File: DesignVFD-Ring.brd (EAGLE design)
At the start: 160 x 100 mm, 33 parts, among them IC1 LMR64010XMF/NOPB, IC2 LM340S-05, J1 NPPN081BFLD-RC, J2 NPPN081BFLD-RC, J3 NPPN081BFLD-RC, J4 NPPN081BFLD-RC, U1 MAX6920AWP+, U2 LM1084IS-5.0, U3 TPS76325DBVT

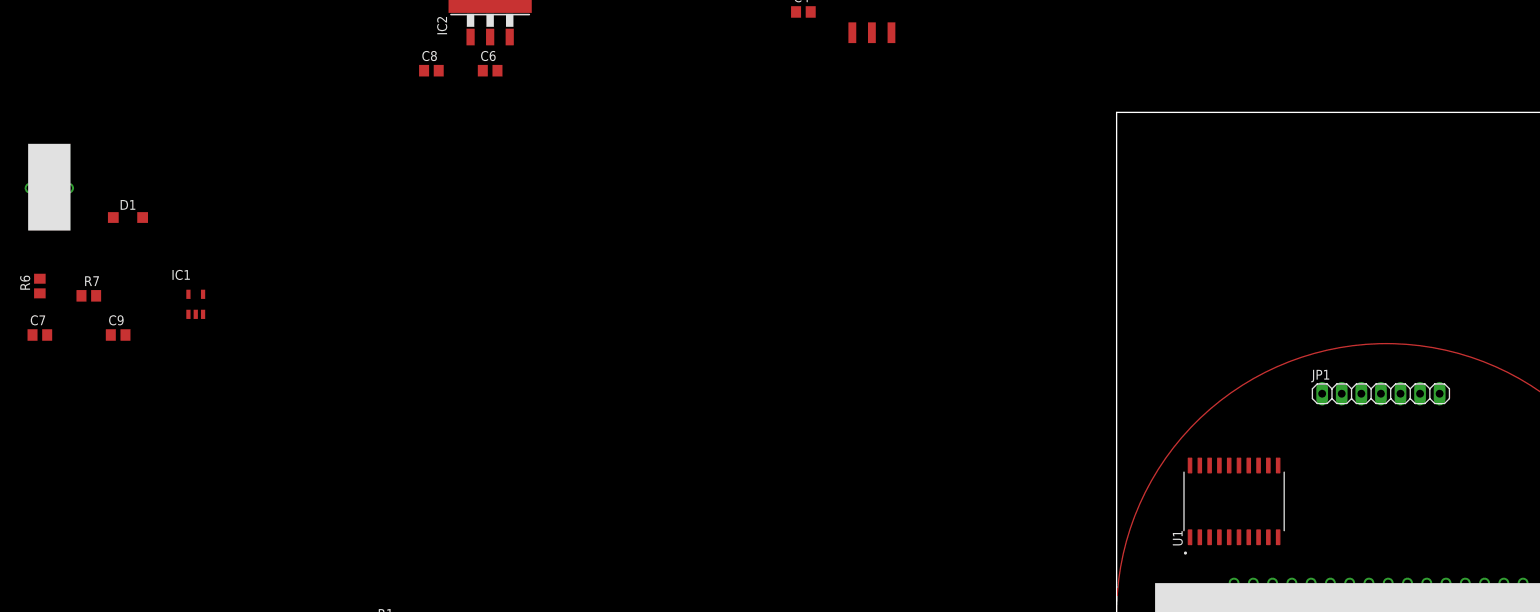
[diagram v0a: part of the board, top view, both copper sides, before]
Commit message: 24V reg layout
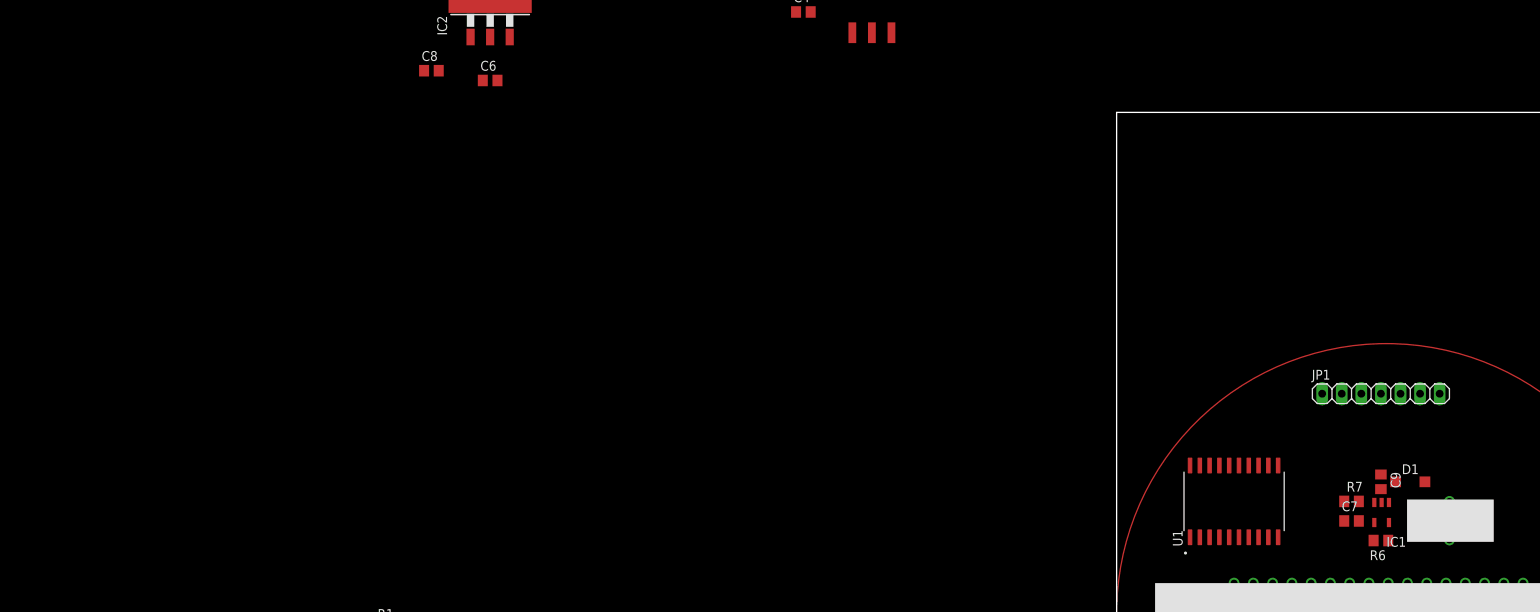
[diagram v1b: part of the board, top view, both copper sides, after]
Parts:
- moved U$1 188.6 mm to (43.2, 49.5), turned to 270 degrees
- moved R6 177.1 mm to (34.3, 44.5), turned to 180 degrees
- moved C7 171.9 mm to (30.5, 47.0)
- moved D1 169.9 mm to (38.1, 52.1)
- moved R7 166.0 mm to (30.5, 49.5)
- moved C9 164.9 mm to (34.3, 52.1), turned to 270 degrees
- moved IC1 156.0 mm to (34.3, 48.3), turned to 180 degrees
- moved C6 1.27 mm to (-81.3, 104.1)

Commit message: Replaced headers with Teensy device
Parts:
- removed J1, J2, J3, J4: NPPN081BFLD-RC, NPPN081BFLD-RC:SULLINS_NPPN081BFLD-RC
- added U$3: TEENSY-3.2, FormE:TEENSY3.2
- moved R2 35.1 mm to (57.1, 47.0)
- moved R3 31.7 mm to (61.0, 45.7), flipped to the bottom, turned to 270 degrees
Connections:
- net +3V3: now also U$3.3V3+; no longer J3.3
- net +5V: now also U$3.VIN; no longer J3.1
- net GND: now also U$3.AGND, U$3.GND; no longer J1.1, J3.2
- net T_BLANK: now also U$3.9; no longer J3.4
- net T_CS2: now also U$3.5; no longer J1.5
- net T_HEATER_CTL: now also U$3.21; no longer J3.6
- net T_IGN_INPUT: now also U$3.7; no longer J1.8
- net T_LIGHT_INPUT: now also U$3.15; no longer J4.4
- net T_MOSI: now also U$3.11; no longer J2.5
- net T_MOSI2: now also U$3.3; no longer J1.4
- net T_SCK: now also U$3.13; no longer J4.6
- net T_SCK2: now also U$3.1; no longer J1.3

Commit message: Initial layout complete
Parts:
- moved C2 177.0 mm to (49.5, 63.8), flipped to the bottom
- moved D3 166.8 mm to (50.8, 59.2)
- moved D2 165.7 mm to (50.8, 55.1)
- moved OK1 164.8 mm to (50.8, 56.9), flipped to the bottom
- moved JP2 163.8 mm to (61.0, 55.1)
- moved U$3 155.5 mm to (29.0, 40.4), flipped to the bottom, turned to 180 degrees
- moved R1 155.1 mm to (57.9, 57.4), flipped to the bottom, turned to 270 degrees
- moved C1 151.6 mm to (52.1, 50.3), flipped to the bottom
- moved IC2 132.1 mm to (15.2, 25.4), flipped to the bottom, turned to 90 degrees
- moved U2 127.9 mm to (33.0, 9.14), flipped to the bottom, turned to 90 degrees
- moved C3 124.0 mm to (21.3, 12.7), flipped to the bottom, turned to 90 degrees
- moved C6 123.7 mm to (9.40, 20.1), flipped to the bottom, turned to 90 degrees
- moved C8 123.6 mm to (9.40, 30.5), flipped to the bottom, turned to 270 degrees
- moved C4 122.1 mm to (21.3, 7.87), flipped to the bottom, turned to 270 degrees
- moved U3 120.1 mm to (51.1, 12.2), flipped to the bottom, turned to 180 degrees
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
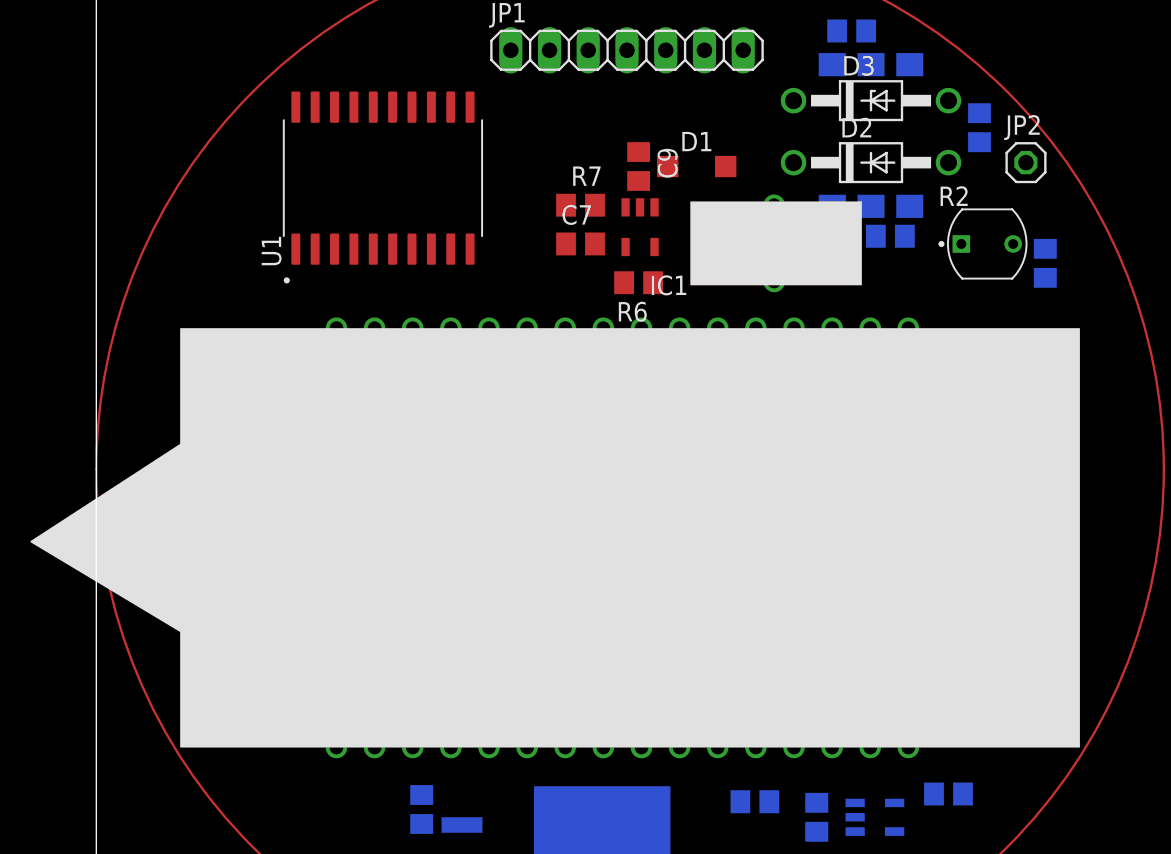
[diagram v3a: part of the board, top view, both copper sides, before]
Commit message: Fine tuned IVL location, added lumini docs
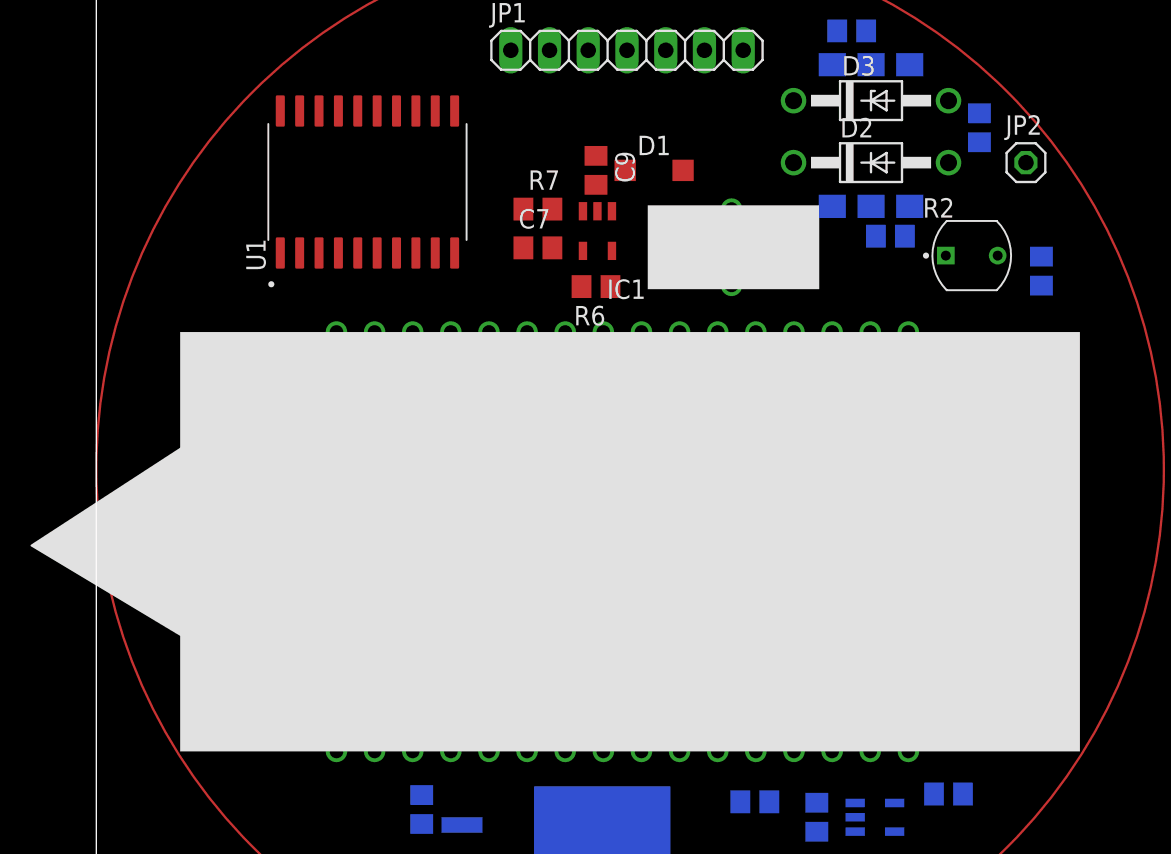
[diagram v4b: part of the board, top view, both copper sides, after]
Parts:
- moved IC1 2.81 mm to (32.8, 50.8)
- moved C9 2.81 mm to (32.8, 54.6)
- moved R6 2.81 mm to (32.8, 47.0)
- moved U$1 2.81 mm to (41.7, 52.1)
- moved C7 2.81 mm to (29.0, 49.5)
- moved R7 2.81 mm to (29.0, 52.1)
- moved D1 2.81 mm to (36.6, 54.6)
- moved R2 1.27 mm to (57.4, 49.0)
- moved U1 1.05 mm to (17.8, 53.8)
- moved R3 0.57 mm to (62.0, 48.0)
- moved U$2 0.25 mm to (15.7, 16.5)

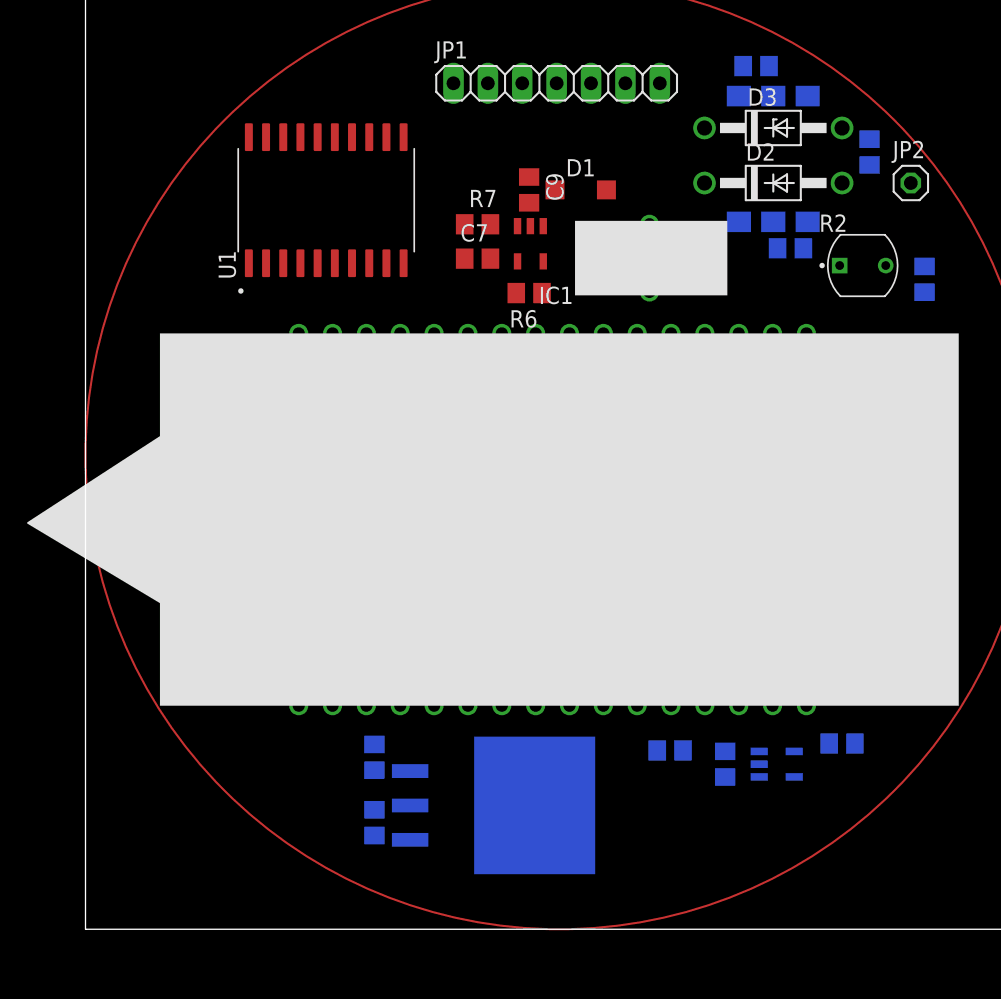
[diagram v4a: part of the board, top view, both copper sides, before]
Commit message: added lumini ring
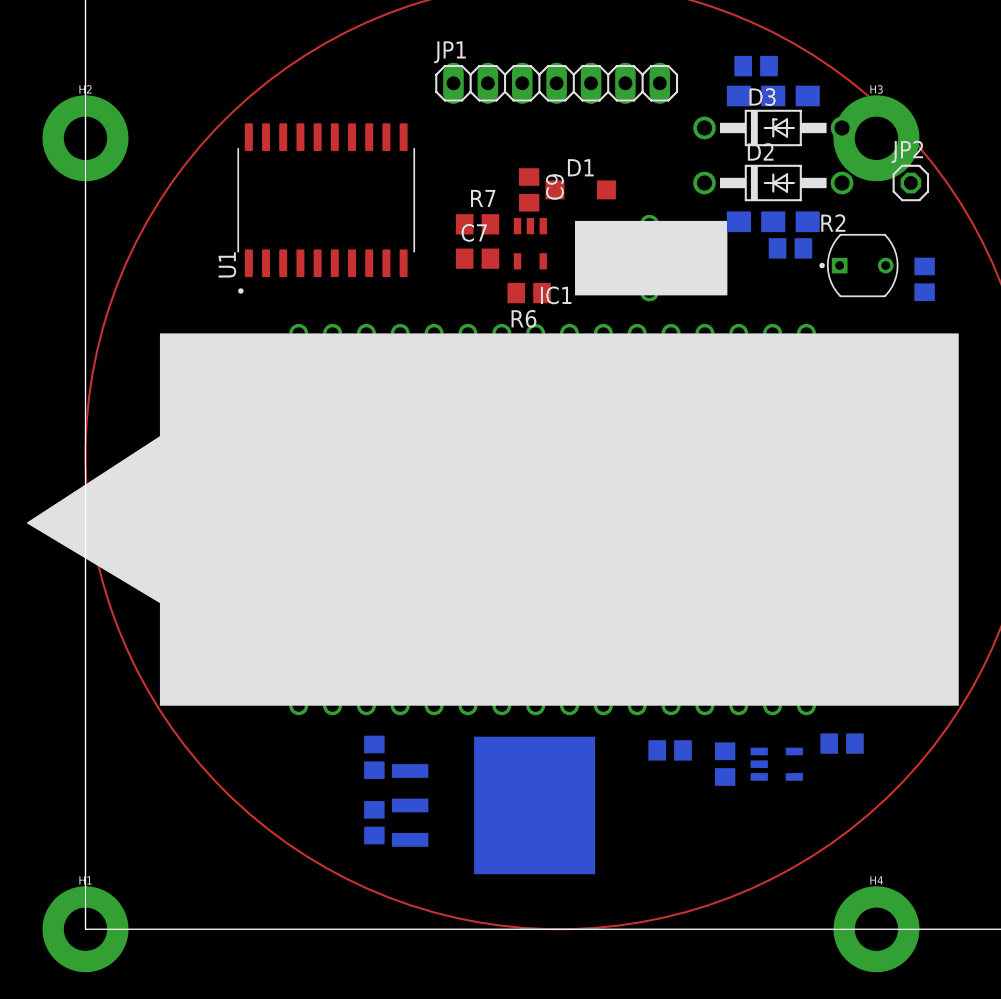
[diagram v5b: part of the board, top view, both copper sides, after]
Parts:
- added H1, H2, H3, H4: STANDOFF_ELECTRICAL, SparkFun-Hardware:STANDOFF-ELECTRICAL
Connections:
- net GND: now also H1.P1, H2.P1, H3.P1, H4.P1

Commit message: about to repin IVL
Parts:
- removed H1, H2, H3, H4: STANDOFF_ELECTRICAL, SparkFun-Hardware:STANDOFF-ELECTRICAL
- added JP3: (no value), pinhead:1X01
- added U$4: LUMINI3, FormE:STANDOFF-ELECTRICAL
- moved R3 47.6 mm to (34.8, 8.89), turned to 0 degrees
- moved R2 43.2 mm to (34.7, 12.2)
- moved C2 12.3 mm to (48.0, 51.6), turned to 270 degrees
- moved JP2 11.9 mm to (58.7, 66.8), turned to 90 degrees
- moved C1 10.1 mm to (61.5, 54.1), turned to 270 degrees
- moved C4 8.52 mm to (13.2, 10.4), turned to 0 degrees
- moved C3 7.18 mm to (14.2, 13.7)
- moved U2 6.88 mm to (26.2, 9.65)
- moved D3 6.59 mm to (52.6, 52.8), turned to 90 degrees
- moved C8 6.55 mm to (5.59, 35.8), turned to 90 degrees
- moved D2 6.27 mm to (56.6, 52.8), turned to 90 degrees
- moved IC2 6.15 mm to (11.4, 30.2)
- moved C6 6.15 mm to (5.59, 24.9), turned to 270 degrees
- moved OK1 5.75 mm to (54.9, 52.8), turned to 270 degrees
- moved R1 5.01 mm to (53.6, 59.9), turned to 180 degrees
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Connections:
- net +15V: now also JP3.1
- net GND: now also U$4.P1, U$4.P2, U$4.P3, U$4.P4; no longer H1.P1, H2.P1, H3.P1, H4.P1
- net T_CS2: now also U$3.3; no longer U$3.5
- net T_MOSI2: now also U$3.5; no longer U$3.3
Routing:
- net T_SCK: track 0.00 -> 59.1 mm, vias 0 -> 1
- net +12V: track 0.00 -> 51.3 mm, vias 0 -> 3
- net N$12: track 0.00 -> 48.5 mm, vias 0 -> 1
- net T_MOSI: track 0.00 -> 45.1 mm, vias 0 -> 1
- net T_CS2: track 0.00 -> 36.7 mm, vias 0 -> 1
- net +3V3: track 0.00 -> 34.7 mm, vias 0 -> 3
- net T_SCK2: track 0.00 -> 33.3 mm, vias 0 -> 1
- net +15V: track 0.00 -> 29.8 mm
- net T_MOSI2: track 0.00 -> 28.0 mm, vias 0 -> 1
- net +24V: track 0.00 -> 23.6 mm
- net N$4: track 0.00 -> 10.7 mm
- net IGN_INPUT: track 0.00 -> 9.73 mm
- net V+: track 0.00 -> 8.15 mm
- net T_HEATER_CTL: track 0.00 -> 7.86 mm
- net N$5: track 0.00 -> 7.25 mm
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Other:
- board size 160 x 100 mm -> 70.1 x 70.1 mm

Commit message: IVL complete
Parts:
- moved C8 6.91 mm to (7.62, 29.2)
- moved IC2 6.59 mm to (13.2, 23.9)
- moved C6 6.11 mm to (7.37, 19.1)
- moved JP2 1.78 mm to (58.7, 65.0)
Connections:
- removed net N$10: U$2.P$4, U1.15
- removed net N$11: U$2.P$5, U1.14
- removed net N$12: U$2.P$7, U1.13
- removed net N$13: U$2.P$10, U1.8
- removed net N$14: U$2.P$2, U1.7
- removed net N$15: U$2.P$6, U1.6
- removed net N$16: U$2.P$11, U1.5
- removed net N$17: U$2.P$15, U1.4
- removed net N$5: U$2.P$14, U1.18
- removed net N$8: U$2.P$13, U1.17
- removed net N$9: U$2.P$12, U1.16
- new net BDOT: U$2.P$9
- new net G1: U$2.P$2, U1.13
- new net G2: U$2.P$6, U1.16
- new net G3: U$2.P$8
- new net G4: U$2.P$11, U1.3
- new net G5: U$2.P$15, U1.7
- new net LOW: U$2.P$10, U1.18
- new net LOW_L: U$2.P$5, U1.15
- new net LOW_R: U$2.P$7, U1.17
- new net MID: U$2.P$4, U1.14
- new net NC: U1.8
- new net TDOT: U$2.P$3
- new net TOP: U$2.P$14, U1.6
- new net TOP_L: U$2.P$13, U1.5
- new net TOP_R: U$2.P$12, U1.4
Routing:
- net G5: track 0.00 -> 78.6 mm
- net TOP: track 0.00 -> 75.0 mm
- net TOP_L: track 0.00 -> 71.0 mm
- net TOP_R: track 0.00 -> 67.4 mm
- net G4: track 0.00 -> 65.3 mm
- net T_BLANK: track 0.00 -> 60.4 mm, vias 0 -> 1
- net T_SCK: track 59.1 -> 1.52 mm, vias 1 -> 0
- net N$12: track 48.5 -> 0.00 mm, vias 1 -> 0
- net T_MOSI: track 45.1 -> 3.59 mm, vias 1 -> 0
- net LOW: track 0.00 -> 39.3 mm
- net LOW_L: track 0.00 -> 39.1 mm
- net +12V: track 51.3 -> 12.6 mm, vias 3 -> 1
- net MID: track 0.00 -> 38.2 mm
- net G2: track 0.00 -> 37.4 mm
- net LOW_R: track 0.00 -> 37.0 mm
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
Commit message: Passed ERC and DRC!
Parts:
- added JP4: (no value), pinhead:1X01
- moved C7 5.38 mm to (27.2, 56.1), turned to 270 degrees
- moved R6 3.06 mm to (29.2, 52.1), turned to 90 degrees
- moved R7 3.06 mm to (29.2, 56.1), turned to 270 degrees
- moved D1 2.05 mm to (38.6, 54.9)
- moved C9 1.27 mm to (32.8, 55.9)
- moved U$1 1.27 mm to (40.4, 52.1)
- moved IC1 0.36 mm to (32.5, 51.1)
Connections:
- net GND: now also JP4.1
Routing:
- net T_SCK: track 1.52 -> 82.0 mm
- net T_MOSI: track 3.59 -> 68.0 mm
- net +12V: track 12.6 -> 70.3 mm
- net GND: track 0.00 -> 23.5 mm, vias 0 -> 19
- net T_IGN_INPUT: track 2.35 -> 16.6 mm
- net +24V: track 23.6 -> 14.7 mm
- net T_LIGHT_INPUT: track 29.3 -> 37.9 mm, vias 1 -> 0
- net N$6: track 4.23 -> 11.6 mm
- net N$7: track 0.00 -> 7.04 mm
- net +3V3: track 50.7 -> 45.4 mm, vias 3 -> 1
- net +5V: track 5.65 -> 3.13 mm
- net T_SCK2: track 33.3 -> 35.2 mm
- net G1: track 36.5 -> 36.0 mm
- added copper zone on layer 16, net +5V
- added copper zone on layer 1, net GND
- added copper zone on layer 16, net GND
